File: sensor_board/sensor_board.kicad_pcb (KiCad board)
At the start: 2 copper layers, 8.2 x 15 mm, 5 parts, among them J1 Conn_01x03, Q1 Q_Photo_NPN_EBC

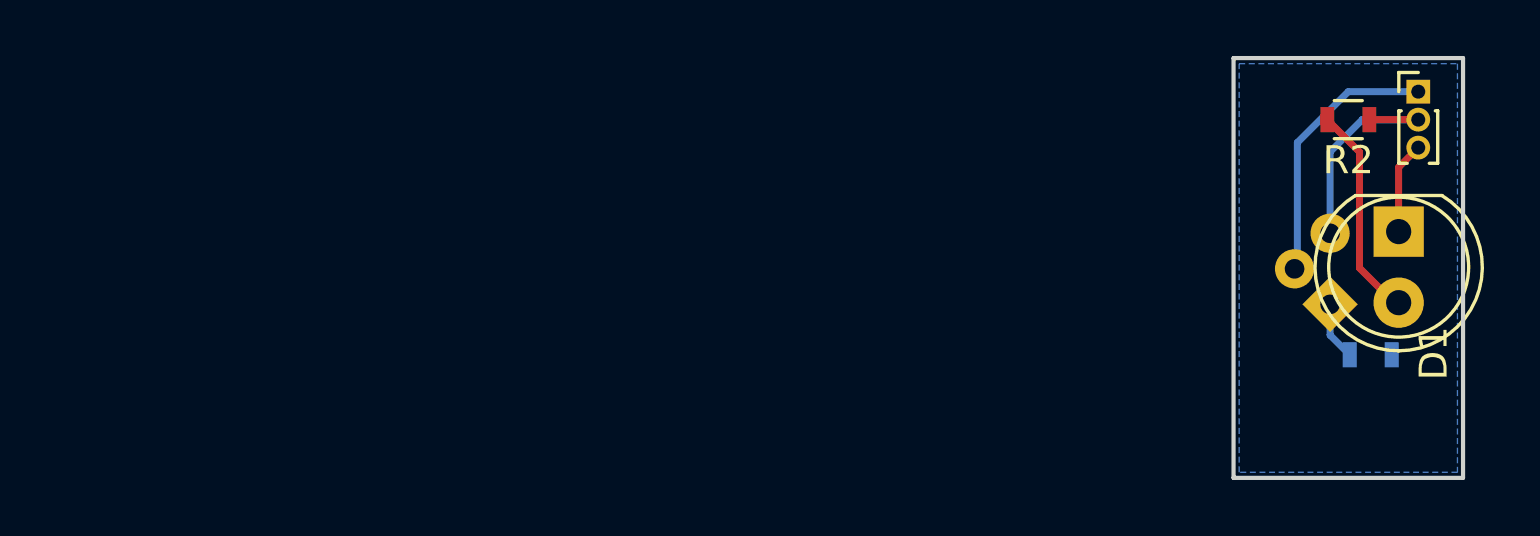
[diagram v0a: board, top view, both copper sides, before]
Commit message: add mounting holes and improve silkscreen
 - board top left is at 100,100
 - overall board size is 7.5mm by 15mm
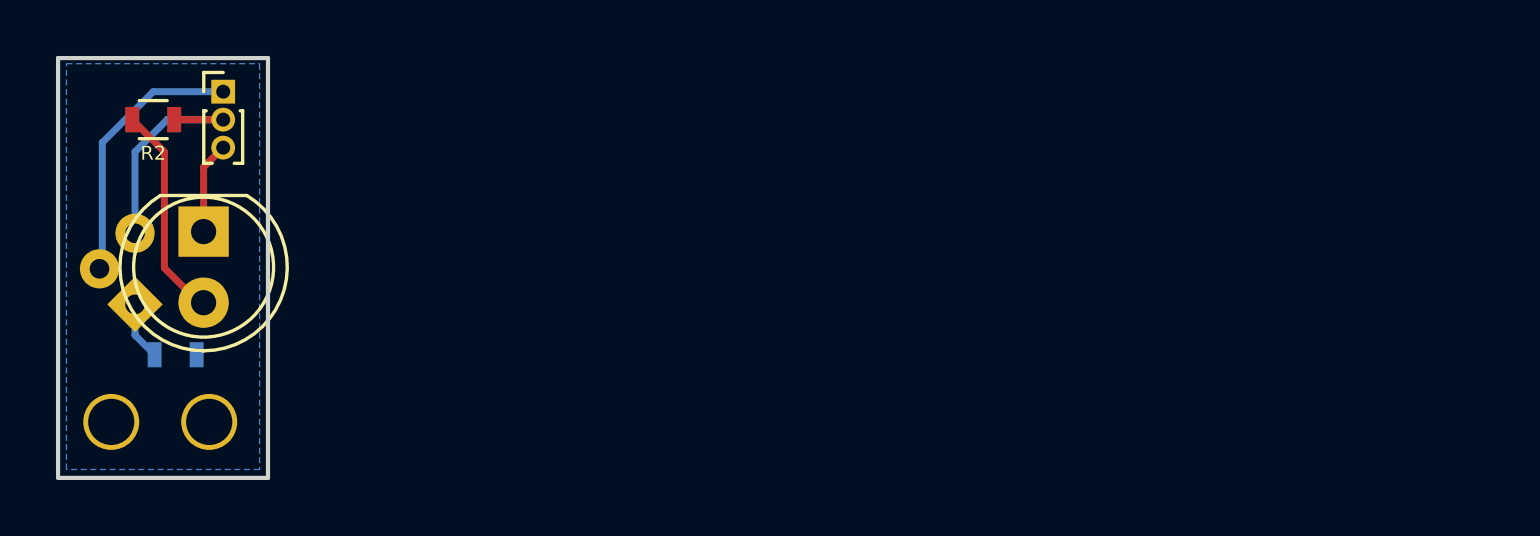
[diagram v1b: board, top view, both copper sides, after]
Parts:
- added REF**: 1pin, sensor_board_custom:1.5mm_mounting_hole, F.Cu at (102.0, 113.0)
- added REF**: 1pin, sensor_board_custom:1.5mm_mounting_hole, F.Cu at (105.5, 113.0)
- moved D1 42.7 mm to (105.2, 106.2)
- moved R1 42.7 mm to (104.2, 110.6)
- moved J1 42.7 mm to (105.9, 101.2)
- moved Q1 42.7 mm to (102.8, 108.8)
- moved R2 42.7 mm to (103.4, 102.2)
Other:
- board size 8.2 x 15 mm -> 7.5 x 15 mm
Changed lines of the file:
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@@
     (links 7)
     (no_connects 0)
-    (area 141.924999 99.924999 150.275001 115.075001)
+    (area 99.924999 99.924999 107.575001 115.075001)
     (thickness 1.6)
     (drawings 4)
     (tracks 18)
     (zones 0)
-    (modules 5)
+    (modules 7)
     (nets 6)
   )
@@
     (mod_text_size 1 1)
     (mod_text_width 0.15)
-    (pad_size 1.524 1.524)
-    (pad_drill 0.762)
+    (pad_size 2 2)
+    (pad_drill 1.65)
     (pad_to_mask_clearance 0.2)
     (aux_axis_origin 0 0)
@@
   )
   (module LEDs:LED_D5.0mm (layer F.Cu)
-    (at 147.9 106.2 270)
+    (at 105.2 106.2 270)
     (descr "LED, diameter 5.0mm, 2 pins, http://cdn-reichelt.de/documents/datenblatt/A500/LL-504BC2E-009.pdf")
     (tags "LED diameter 5.0mm 2 pins")
-    (fp_text reference D1 (at 4.35 -1.25 270) (layer F.SilkS)
+    (fp_text reference D1 (at 4.35 -1.25 270) (layer F.SilkS) hide
       (effects (font (size 1 1) (thickness 0.15)))
     )
@@
   )
   (module Pin_Headers:Pin_Header_Straight_1x03_Pitch1.00mm (layer F.Cu)
-    (at 148.6 101.2)
+    (at 105.9 101.2)
     (descr "Through hole straight pin header, 1x03, 1.00mm pitch, single row")
     (tags "Through hole pin header THT 1x03 1.00mm single row")
@@
   )
   (module "Opto-Devices:LaserDiode_TO5(D9)-3" (layer B.Cu)
-    (at 145.45 108.8 90)
+    (at 102.75 108.8 90)
     (descr "Laser Diode, TO5-like (D=9mm), 3pin")
     (tags "Laser Diode TO5-like")
@@
   )
   (module Resistors_SMD:R_0603 (layer B.Cu)
-    (at 146.9 110.6)
+    (at 104.2 110.6)
     (descr "Resistor SMD 0603, reflow soldering, Vishay (see dcrcw.pdf)")
     (tags "resistor 0603")
     (attr smd)
-    (fp_text reference R1 (at 0 1.45) (layer B.SilkS)
-      (effects (font (size 1 1) (thickness 0.15)) (justify mirror))
+    (fp_text reference R1 (at -0.1 1.1) (layer B.SilkS)
+      (effects (font (size 0.5 0.5) (thickness 0.125)) (justify mirror))
     )
     (fp_text value R (at 0 -1.5) (layer B.Fab)
@@
   )
   (module Resistors_SMD:R_0603 (layer F.Cu)
-    (at 146.1 102.2 180)
+    (at 103.4 102.2 180)
     (descr "Resistor SMD 0603, reflow soldering, Vishay (see dcrcw.pdf)")
     (tags "resistor 0603")
     (attr smd)
-    (fp_text reference R2 (at 0 -1.45 180) (layer F.SilkS)
-      (effects (font (size 1 1) (thickness 0.15)))
+    (fp_text reference R2 (at 0 -1.2 180) (layer F.SilkS)
+      (effects (font (size 0.5 0.5) (thickness 0.125)))
     )
     (fp_text value R (at 0 1.5 180) (layer F.Fab)
@@
     )
   )
-  (gr_line (start 142 100) (end 150.2 100) (angle 90) (layer Edge.Cuts) (width 0.15))
-  (gr_line (start 142 115) (end 142 100) (angle 90) (layer Edge.Cuts) (width 0.15))
-  (gr_line (start 150.2 115) (end 142 115) (angle 90) (layer Edge.Cuts) (width 0.15))
-  (gr_line (start 150.2 100) (end 150.2 115) (angle 90) (layer Edge.Cuts) (width 0.15))
-  (segment (start 147.9 106.2) (end 147.9 103.9) (width 0.25) (layer F.Cu) (net 1))
-  (segment (start 147.9 103.9) (end 148.6 103.2) (width 0.25) (layer F.Cu) (net 1))
-  (segment (start 148.7 103.3) (end 148.7 103.2) (width 0.25) (layer B.Cu) (net 1))
-  (segment (start 147.9 108.74) (end 147.74 108.74) (width 0.25) (layer F.Cu) (net 2))
-  (segment (start 147.74 108.74) (end 146.5 107.5) (width 0.25) (layer F.Cu) (net 2))
-  (segment (start 146.5 107.5) (end 146.5 103.35) (width 0.25) (layer F.Cu) (net 2))
-  (segment (start 146.5 103.35) (end 145.35 102.2) (width 0.25) (layer F.Cu) (net 2))
-  (segment (start 147.7 108.74) (end 147.64 108.74) (width 0.25) (layer F.Cu) (net 2))
-  (segment (start 148.8 102.2) (end 146.85 102.2) (width 0.25) (layer F.Cu) (net 3))
-  (segment (start 145.45 106.26) (end 145.45 103.35) (width 0.25) (layer B.Cu) (net 3))
-  (segment (start 145.45 103.35) (end 146.6 102.2) (width 0.25) (layer B.Cu) (net 3))
-  (segment (start 146.6 102.2) (end 148.8 102.2) (width 0.25) (layer B.Cu) (net 3))
-  (segment (start 146.6 102.2) (end 148.7 102.2) (width 0.25) (layer B.Cu) (net 3))
-  (segment (start 144.28 107.53) (end 144.28 103.02) (width 0.25) (layer B.Cu) (net 4))
-  (segment (start 146.1 101.2) (end 148.8 101.2) (width 0.25) (layer B.Cu) (net 4))
-  (segment (start 144.28 103.02) (end 146.1 101.2) (width 0.25) (layer B.Cu) (net 4))
-  (segment (start 145.45 108.8) (end 145.45 109.9) (width 0.25) (layer B.Cu) (net 5))
-  (segment (start 145.45 109.9) (end 146.15 110.6) (width 0.25) (layer B.Cu) (net 5))
+  (module sensor_board_custom:1.5mm_mounting_hole (layer F.Cu)
+    (at 102 113)
+    (descr "module 1 pin (ou trou mecanique de percage)")
+    (tags DEV)
+    (fp_text reference REF** (at 0 -3.048) (layer F.SilkS) hide
+      (effects (font (size 1 1) (thickness 0.15)))
+    )
+    (fp_text value 1pin (at 0 3) (layer F.Fab)
+      (effects (font (size 1 1) (thickness 0.15)))
+    )
+    (fp_circle (center 0 0) (end 2 0.8) (layer F.Fab) (width 0.1))
+    (fp_circle (center 0 0) (end 2.6 0) (layer F.CrtYd) (width 0.05))
+    (pad "" np_thru_hole circle (at -0.1 0) (size 2 2) (drill 1.65) (layers *.Cu *.Mask))
+  )
+  (module sensor_board_custom:1.5mm_mounting_hole (layer F.Cu)
+    (at 105.5 113)
+    (descr "module 1 pin (ou trou mecanique de percage)")
+    (tags DEV)
+    (fp_text reference REF** (at 0 -3.048) (layer F.SilkS) hide
+      (effects (font (size 1 1) (thickness 0.15)))
+    )
+    (fp_text value 1pin (at 0 3) (layer F.Fab)
+      (effects (font (size 1 1) (thickness 0.15)))
+    )
+    (fp_circle (center 0 0) (end 2 0.8) (layer F.Fab) (width 0.1))
+    (fp_circle (center 0 0) (end 2.6 0) (layer F.CrtYd) (width 0.05))
+    (pad "" np_thru_hole circle (at -0.1 0) (size 2 2) (drill 1.65) (layers *.Cu *.Mask))
+  )
+  (gr_line (start 100 100) (end 107.5 100) (angle 90) (layer Edge.Cuts) (width 0.15))
+  (gr_line (start 100 115) (end 100 100) (angle 90) (layer Edge.Cuts) (width 0.15))
+  (gr_line (start 107.5 115) (end 100 115) (angle 90) (layer Edge.Cuts) (width 0.15))
+  (gr_line (start 107.5 100) (end 107.5 115) (angle 90) (layer Edge.Cuts) (width 0.15))
+  (segment (start 105.2 106.2) (end 105.2 103.9) (width 0.25) (layer F.Cu) (net 1))
+  (segment (start 105.2 103.9) (end 105.9 103.2) (width 0.25) (layer F.Cu) (net 1))
+  (segment (start 106 103.3) (end 106 103.2) (width 0.25) (layer B.Cu) (net 1))
+  (segment (start 105.2 108.74) (end 105.04 108.74) (width 0.25) (layer F.Cu) (net 2))
+  (segment (start 105.04 108.74) (end 103.8 107.5) (width 0.25) (layer F.Cu) (net 2))
+  (segment (start 103.8 107.5) (end 103.8 103.35) (width 0.25) (layer F.Cu) (net 2))
+  (segment (start 103.8 103.35) (end 102.65 102.2) (width 0.25) (layer F.Cu) (net 2))
+  (segment (start 105 108.74) (end 104.94 108.74) (width 0.25) (layer F.Cu) (net 2))
+  (segment (start 106.1 102.2) (end 104.15 102.2) (width 0.25) (layer F.Cu) (net 3))
+  (segment (start 102.75 106.26) (end 102.75 103.35) (width 0.25) (layer B.Cu) (net 3))
+  (segment (start 102.75 103.35) (end 103.9 102.2) (width 0.25) (layer B.Cu) (net 3))
+  (segment (start 103.9 102.2) (end 106.1 102.2) (width 0.25) (layer B.Cu) (net 3))
+  (segment (start 103.9 102.2) (end 106 102.2) (width 0.25) (layer B.Cu) (net 3))
+  (segment (start 101.58 107.53) (end 101.58 103.02) (width 0.25) (layer B.Cu) (net 4))
+  (segment (start 103.4 101.2) (end 106.1 101.2) (width 0.25) (layer B.Cu) (net 4))
+  (segment (start 101.58 103.02) (end 103.4 101.2) (width 0.25) (layer B.Cu) (net 4))
+  (segment (start 102.75 108.8) (end 102.75 109.9) (width 0.25) (layer B.Cu) (net 5))
+  (segment (start 102.75 109.9) (end 103.45 110.6) (width 0.25) (layer B.Cu) (net 5))
   (zone (net 1) (net_name GND) (layer B.Cu) (hatch edge 0.508)
     (connect_pads (clearance 0.508))
@@
     (polygon
       (pts
-        (xy 150 114.8) (xy 142.2 114.8) (xy 142.2 100.2) (xy 150 100.2)
+        (xy 107.2 114.7) (xy 100.3 114.7) (xy 100.3 100.2) (xy 107.2 100.2)
       )
     )
